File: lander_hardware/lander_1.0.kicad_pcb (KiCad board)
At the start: 2 copper layers, 76.2 x 63.5 mm, 45 parts, among them IC1 ATMEGA328-P, J1 Power Connector, J3 Pyro Channel, J4 Pyro Channel, J5 Pyro Channel, P1 Power Out, P2 ICSP, P3 XBEE Out, P4 Digital Supplement 1, P5 Digital Supplement 2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

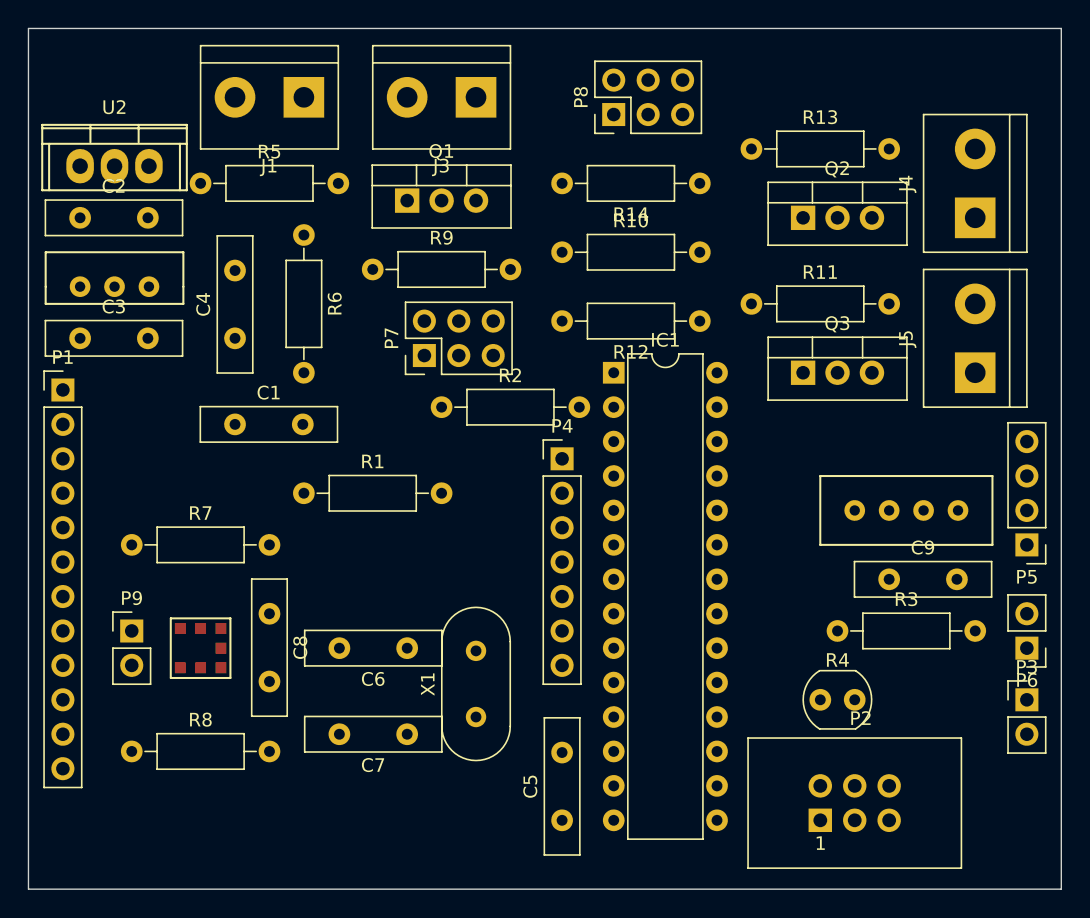
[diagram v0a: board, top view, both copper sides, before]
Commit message: Moved some decoupling caps closer
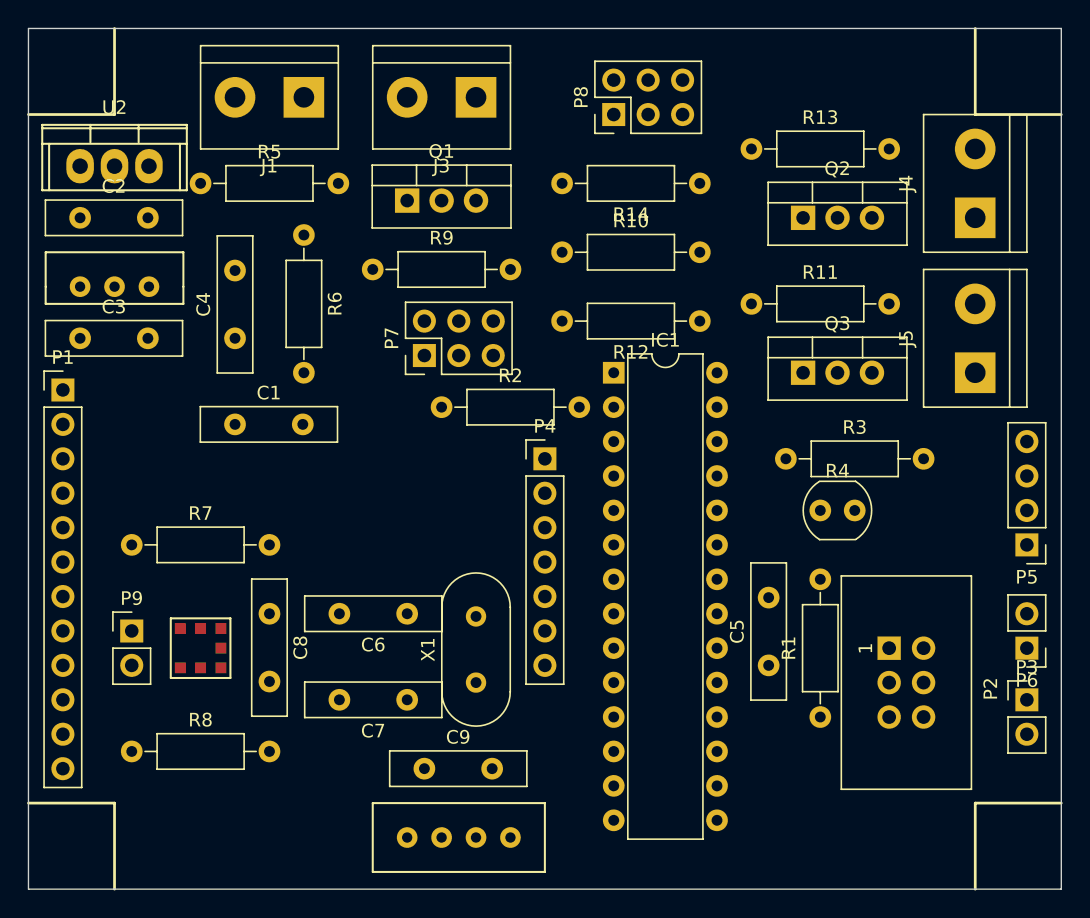
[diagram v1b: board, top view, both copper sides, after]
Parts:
- moved R1 41.5 mm to (196.8, 138.4), turned to 90 degrees
- moved U3 40.9 mm to (170.2, 147.3)
- moved C9 37.0 mm to (167.6, 142.2)
- moved C5 19.0 mm to (193.0, 134.6)
- moved R4 14.0 mm to (196.8, 123.2)
- moved P2 13.7 mm to (201.9, 133.3), turned to 270 degrees
- moved R3 13.3 mm to (194.3, 119.4)
- moved X1 2.54 mm to (171.4, 135.9)
- moved C6 2.54 mm to (166.4, 130.8)
- moved C7 2.54 mm to (166.4, 137.2)
- moved P4 1.27 mm to (176.5, 119.4)
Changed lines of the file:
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@@
     (links 117)
     (no_connects 117)
-    (area 137.912857 86.655 220.313811 152.125)
+    (area 136.912857 86.655 220.313811 152.125)
     (thickness 1.6)
-    (drawings 4)
+    (drawings 12)
     (tracks 0)
     (zones 0)
@@
   )
   (module Capacitors_THT:C_Disc_D10.0mm_W2.5mm_P5.00mm (layer F.Cu)
-    (at 177.8 146.05 90)
+    (at 193.04 134.62 90)
     (descr "C, Disc series, Radial, pin pitch=5.00mm, , diameter*width=10*2.5mm^2, Capacitor, http://cdn-reichelt.de/documents/datenblatt/B300/DS_KERKO_TC.pdf")
     (tags "C Disc series Radial pin pitch 5.00mm  diameter 10mm width 2.5mm Capacitor")
@@
   )
   (module Capacitors_THT:C_Disc_D10.0mm_W2.5mm_P5.00mm (layer F.Cu)
-    (at 166.37 133.35 180)
+    (at 166.37 130.81 180)
     (descr "C, Disc series, Radial, pin pitch=5.00mm, , diameter*width=10*2.5mm^2, Capacitor, http://cdn-reichelt.de/documents/datenblatt/B300/DS_KERKO_TC.pdf")
     (tags "C Disc series Radial pin pitch 5.00mm  diameter 10mm width 2.5mm Capacitor")
@@
   )
   (module Capacitors_THT:C_Disc_D10.0mm_W2.5mm_P5.00mm (layer F.Cu)
-    (at 166.37 139.7 180)
+    (at 166.37 137.16 180)
     (descr "C, Disc series, Radial, pin pitch=5.00mm, , diameter*width=10*2.5mm^2, Capacitor, http://cdn-reichelt.de/documents/datenblatt/B300/DS_KERKO_TC.pdf")
     (tags "C Disc series Radial pin pitch 5.00mm  diameter 10mm width 2.5mm Capacitor")
@@
   )
   (module Capacitors_THT:C_Disc_D10.0mm_W2.5mm_P5.00mm (layer F.Cu)
-    (at 201.93 128.27)
+    (at 167.64 142.24)
     (descr "C, Disc series, Radial, pin pitch=5.00mm, , diameter*width=10*2.5mm^2, Capacitor, http://cdn-reichelt.de/documents/datenblatt/B300/DS_KERKO_TC.pdf")
     (tags "C Disc series Radial pin pitch 5.00mm  diameter 10mm width 2.5mm Capacitor")
@@
   )
   (module Connectors:IDC_Header_Straight_6pins (layer F.Cu)
-    (at 196.85 146.05)
+    (at 201.93 133.35 270)
     (descr "6 pins through hole IDC header")
     (tags "IDC header socket VASCH AVR ISP")
-    (fp_text reference P2 (at 3 -7.5) (layer F.SilkS)
-      (effects (font (size 1 1) (thickness 0.15)))
-    )
-    (fp_text value ICSP (at 3 5) (layer F.Fab)
+    (fp_text reference P2 (at 3 -7.5 270) (layer F.SilkS)
+      (effects (font (size 1 1) (thickness 0.15)))
+    )
+    (fp_text value ICSP (at 3 5 270) (layer F.Fab)
       (effects (font (size 1 1) (thickness 0.15)))
     )
@@
     (fp_line (start 10.66 3.78) (end -5.58 3.78) (layer F.CrtYd) (width 0.05))
     (fp_line (start -5.58 3.78) (end -5.58 -6.32) (layer F.CrtYd) (width 0.05))
-    (fp_text user 1 (at 0.02 1.72) (layer F.SilkS)
+    (fp_text user 1 (at 0.02 1.72 270) (layer F.SilkS)
       (effects (font (size 1 1) (thickness 0.12)))
     )
@@
     (fp_line (start 10.41 3.53) (end -5.33 3.53) (layer F.SilkS) (width 0.12))
     (fp_line (start -5.33 3.53) (end -5.33 -6.07) (layer F.SilkS) (width 0.12))
-    (pad 1 thru_hole rect (at 0 0) (size 1.7272 1.7272) (drill 1.016) (layers *.Cu *.Mask)
+    (pad 1 thru_hole rect (at 0 0 270) (size 1.7272 1.7272) (drill 1.016) (layers *.Cu *.Mask)
       (net 14 "Net-(IC1-Pad18)"))
-    (pad 2 thru_hole oval (at 0 -2.54) (size 1.7272 1.7272) (drill 1.016) (layers *.Cu *.Mask)
+    (pad 2 thru_hole oval (at 0 -2.54 270) (size 1.7272 1.7272) (drill 1.016) (layers *.Cu *.Mask)
       (net 4 +5V))
-    (pad 3 thru_hole oval (at 2.54 0) (size 1.7272 1.7272) (drill 1.016) (layers *.Cu *.Mask)
+    (pad 3 thru_hole oval (at 2.54 0 270) (size 1.7272 1.7272) (drill 1.016) (layers *.Cu *.Mask)
       (net 16 "Net-(IC1-Pad19)"))
-    (pad 4 thru_hole oval (at 2.54 -2.54) (size 1.7272 1.7272) (drill 1.016) (layers *.Cu *.Mask)
+    (pad 4 thru_hole oval (at 2.54 -2.54 270) (size 1.7272 1.7272) (drill 1.016) (layers *.Cu *.Mask)
       (net 12 "Net-(IC1-Pad17)"))
-    (pad 5 thru_hole oval (at 5.08 0) (size 1.7272 1.7272) (drill 1.016) (layers *.Cu *.Mask)
+    (pad 5 thru_hole oval (at 5.08 0 270) (size 1.7272 1.7272) (drill 1.016) (layers *.Cu *.Mask)
       (net 7 "Net-(IC1-Pad1)"))
-    (pad 6 thru_hole oval (at 5.08 -2.54) (size 1.7272 1.7272) (drill 1.016) (layers *.Cu *.Mask)
+    (pad 6 thru_hole oval (at 5.08 -2.54 270) (size 1.7272 1.7272) (drill 1.016) (layers *.Cu *.Mask)
       (net 2 GND))
   )
@@
   )
   (module Pin_Headers:Pin_Header_Straight_1x07_Pitch2.54mm (layer F.Cu)
-    (at 177.8 119.38)
+    (at 176.53 119.38)
     (descr "Through hole straight pin header, 1x07, 2.54mm pitch, single row")
     (tags "Through hole pin header THT 1x07 2.54mm single row")
@@
   )
   (module Resistors_THT:R_Axial_DIN0207_L6.3mm_D2.5mm_P10.16mm_Horizontal (layer F.Cu)
-    (at 158.75 121.92)
+    (at 196.85 138.43 90)
     (descr "Resistor, Axial_DIN0207 series, Axial, Horizontal, pin pitch=10.16mm, 0.25W = 1/4W, length*diameter=6.3*2.5mm^2, http://cdn-reichelt.de/documents/datenblatt/B400/1_4W%23YAG.pdf")
     (tags "Resistor Axial_DIN0207 series Axial Horizontal pin pitch 10.16mm 0.25W = 1/4W length 6.3mm diameter 2.5mm")
-    (fp_text reference R1 (at 5.08 -2.31) (layer F.SilkS)
-      (effects (font (size 1 1) (thickness 0.15)))
-    )
-    (fp_text value 10K (at 5.08 2.31) (layer F.Fab)
+    (fp_text reference R1 (at 5.08 -2.31 90) (layer F.SilkS)
+      (effects (font (size 1 1) (thickness 0.15)))
+    )
+    (fp_text value 10K (at 5.08 2.31 90) (layer F.Fab)
       (effects (font (size 1 1) (thickness 0.15)))
     )
@@
     (fp_line (start 11.25 1.6) (end 11.25 -1.6) (layer F.CrtYd) (width 0.05))
     (fp_line (start 11.25 -1.6) (end -1.05 -1.6) (layer F.CrtYd) (width 0.05))
-    (pad 1 thru_hole circle (at 0 0) (size 1.6 1.6) (drill 0.8) (layers *.Cu *.Mask)
+    (pad 1 thru_hole circle (at 0 0 90) (size 1.6 1.6) (drill 0.8) (layers *.Cu *.Mask)
       (net 4 +5V))
-    (pad 2 thru_hole oval (at 10.16 0) (size 1.6 1.6) (drill 0.8) (layers *.Cu *.Mask)
+    (pad 2 thru_hole oval (at 10.16 0 90) (size 1.6 1.6) (drill 0.8) (layers *.Cu *.Mask)
       (net 18 "Net-(IC1-Pad21)"))
     (model Resistors_THT.3dshapes/R_Axial_DIN0207_L6.3mm_D2.5mm_P10.16mm_Horizontal.wrl
@@
   )
   (module Resistors_THT:R_Axial_DIN0207_L6.3mm_D2.5mm_P10.16mm_Horizontal (layer F.Cu)
-    (at 198.12 132.08)
+    (at 194.31 119.38)
     (descr "Resistor, Axial_DIN0207 series, Axial, Horizontal, pin pitch=10.16mm, 0.25W = 1/4W, length*diameter=6.3*2.5mm^2, http://cdn-reichelt.de/documents/datenblatt/B400/1_4W%23YAG.pdf")
     (tags "Resistor Axial_DIN0207 series Axial Horizontal pin pitch 10.16mm 0.25W = 1/4W length 6.3mm diameter 2.5mm")
@@
   )
   (module Opto-Devices:Resistor_LDR_4.9x4.2_RM2.54 (layer F.Cu)
-    (at 196.85 137.16)
+    (at 196.85 123.19)
     (descr "Resistor, LDR 4.9x4.2mm")
     (tags "Resistor LDR4.9x4.2")
@@
   )
   (module footprints:dht11 (layer F.Cu)
-    (at 203.2 123.19)
+    (at 170.18 147.32)
     (fp_text reference U3 (at 0 2.54) (layer F.SilkS) hide
       (effects (font (size 1 1) (thickness 0.15)))
@@
   )
   (module Crystals:Crystal_HC49-U_Vertical (layer F.Cu)
-    (at 171.45 138.43 90)
+    (at 171.45 135.89 90)
     (descr "Crystal THT HC-49/U http://5hertz.com/pdfs/04404_D.pdf")
     (tags "THT crystalHC-49/U")
@@
       (net 40 "Net-(U4-Pad7)"))
   )
+  (gr_line (start 144.78 144.78) (end 138.43 144.78) (angle 90) (layer F.SilkS) (width 0.2))
+  (gr_line (start 144.78 151.13) (end 144.78 144.78) (angle 90) (layer F.SilkS) (width 0.2))
+  (gr_line (start 208.28 144.78) (end 214.63 144.78) (angle 90) (layer F.SilkS) (width 0.2))
+  (gr_line (start 208.28 151.13) (end 208.28 144.78) (angle 90) (layer F.SilkS) (width 0.2))
+  (gr_line (start 208.28 93.98) (end 208.28 87.63) (angle 90) (layer F.SilkS) (width 0.2))
+  (gr_line (start 214.63 93.98) (end 208.28 93.98) (angle 90) (layer F.SilkS) (width 0.2))
+  (gr_line (start 144.78 93.98) (end 144.78 87.63) (angle 90) (layer F.SilkS) (width 0.2))
+  (gr_line (start 138.43 93.98) (end 144.78 93.98) (angle 90) (layer F.SilkS) (width 0.2))
   (gr_line (start 138.43 151.13) (end 138.43 87.63) (angle 90) (layer Edge.Cuts) (width 0.1))
   (gr_line (start 214.63 151.13) (end 138.43 151.13) (angle 90) (layer Edge.Cuts) (width 0.1))

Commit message: Updated constraints
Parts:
- moved R9 1.27 mm to (162.6, 105.4)
- moved P8 1.27 mm to (181.6, 95.2)
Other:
- net class 6V Power added: clearance 0.2, trace_width 0.8, via_dia 0.6, via_drill 0.4
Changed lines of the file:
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@@
     (links 117)
     (no_connects 117)
-    (area 136.912857 86.655 220.313811 152.125)
+    (area 136.912857 86.655 220.313811 151.230001)
     (thickness 1.6)
     (drawings 12)
@@
     (add_net +3V3)
     (add_net +5V)
-    (add_net +6V)
     (add_net "/Altimeter I2C/SCL")
     (add_net "/Altimeter I2C/SDA")
@@
     (add_net "Net-(U4-Pad7)")
   )
+  (net_class "6V Power" ""
+    (clearance 0.2)
+    (trace_width 0.8)
+    (via_dia 0.6)
+    (via_drill 0.4)
+    (uvia_dia 0.3)
+    (uvia_drill 0.1)
+    (add_net +6V)
+  )
   (module Capacitors_THT:C_Disc_D10.0mm_W2.5mm_P5.00mm (layer F.Cu)
     (at 153.67 116.84)
@@
     (descr "28-lead dip package, row spacing 7.62 mm (300 mils)")
     (tags "DIL DIP PDIP 2.54mm 7.62mm 300mil")
-    (fp_text reference IC1 (at 3.81 -2.39) (layer F.SilkS)
+    (fp_text reference IC1 (at 3.81 1.27) (layer F.SilkS)
       (effects (font (size 1 1) (thickness 0.15)))
     )
@@
   )
   (module Pin_Headers:Pin_Header_Straight_2x03_Pitch2.54mm (layer F.Cu)
-    (at 181.61 93.98 90)
+    (at 181.61 95.25 90)
     (descr "Through hole straight pin header, 2x03, 2.54mm pitch, double rows")
     (tags "Through hole pin header THT 2x03 2.54mm double row")
@@
   )
   (module Resistors_THT:R_Axial_DIN0207_L6.3mm_D2.5mm_P10.16mm_Horizontal (layer F.Cu)
-    (at 163.83 105.41)
+    (at 162.56 105.41)
     (descr "Resistor, Axial_DIN0207 series, Axial, Horizontal, pin pitch=10.16mm, 0.25W = 1/4W, length*diameter=6.3*2.5mm^2, http://cdn-reichelt.de/documents/datenblatt/B400/1_4W%23YAG.pdf")
     (tags "Resistor Axial_DIN0207 series Axial Horizontal pin pitch 10.16mm 0.25W = 1/4W length 6.3mm diameter 2.5mm")
@@
     (descr "Resistor, Axial_DIN0207 series, Axial, Horizontal, pin pitch=10.16mm, 0.25W = 1/4W, length*diameter=6.3*2.5mm^2, http://cdn-reichelt.de/documents/datenblatt/B400/1_4W%23YAG.pdf")
     (tags "Resistor Axial_DIN0207 series Axial Horizontal pin pitch 10.16mm 0.25W = 1/4W length 6.3mm diameter 2.5mm")
-    (fp_text reference R10 (at 5.08 -2.31) (layer F.SilkS)
+    (fp_text reference R10 (at 5.08 0) (layer F.SilkS)
       (effects (font (size 1 1) (thickness 0.15)))
     )
@@
     (descr "Resistor, Axial_DIN0207 series, Axial, Horizontal, pin pitch=10.16mm, 0.25W = 1/4W, length*diameter=6.3*2.5mm^2, http://cdn-reichelt.de/documents/datenblatt/B400/1_4W%23YAG.pdf")
     (tags "Resistor Axial_DIN0207 series Axial Horizontal pin pitch 10.16mm 0.25W = 1/4W length 6.3mm diameter 2.5mm")
-    (fp_text reference R12 (at 5.08 -2.31 180) (layer F.SilkS)
+    (fp_text reference R12 (at 5.08 0 180) (layer F.SilkS)
       (effects (font (size 1 1) (thickness 0.15)))
     )
@@
     (descr "Resistor, Axial_DIN0207 series, Axial, Horizontal, pin pitch=10.16mm, 0.25W = 1/4W, length*diameter=6.3*2.5mm^2, http://cdn-reichelt.de/documents/datenblatt/B400/1_4W%23YAG.pdf")
     (tags "Resistor Axial_DIN0207 series Axial Horizontal pin pitch 10.16mm 0.25W = 1/4W length 6.3mm diameter 2.5mm")
-    (fp_text reference R14 (at 5.08 -2.31 180) (layer F.SilkS)
-      (effects (font (size 1 1) (thickness 0.15)))
-    )
+    (fp_text reference R14 (at 5.08 0 180) (layer F.SilkS)
+      (effects (font (size 1 1) (thickness 0.15)))
+    )

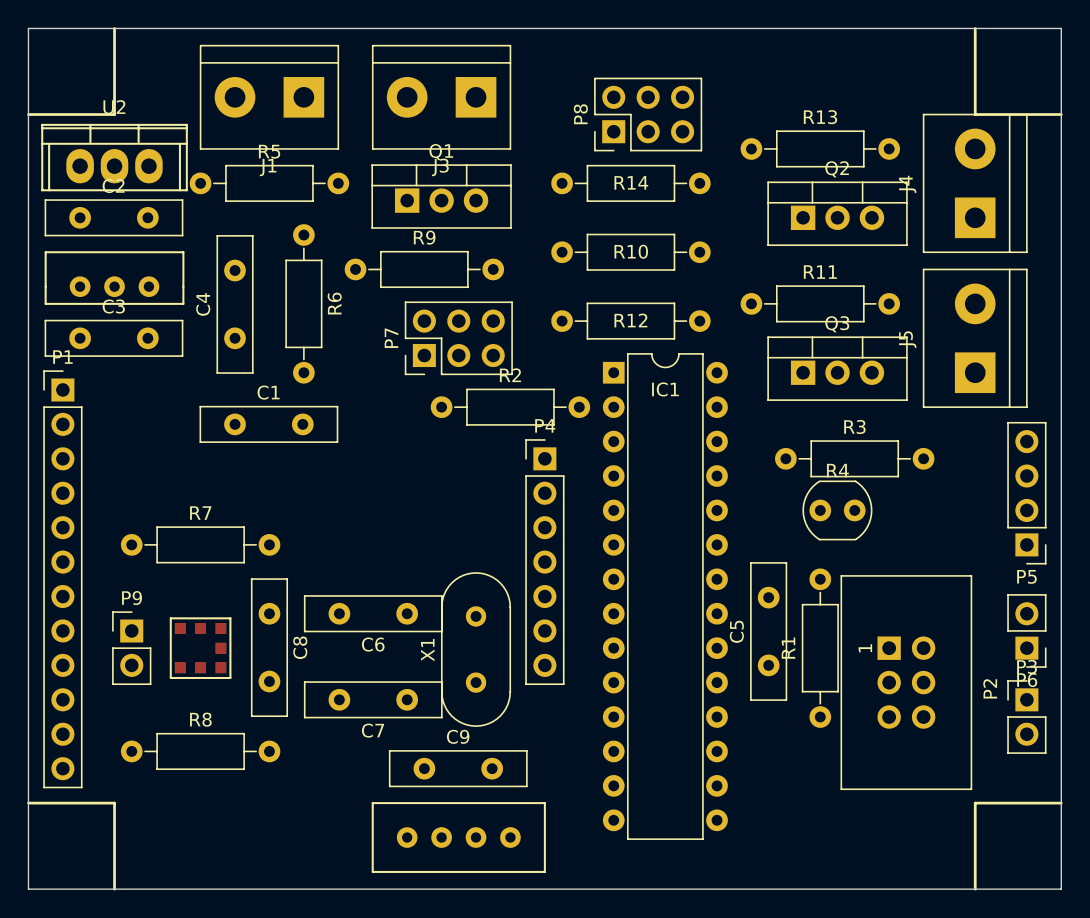
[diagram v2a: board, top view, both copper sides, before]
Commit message: Track width, via size, screws
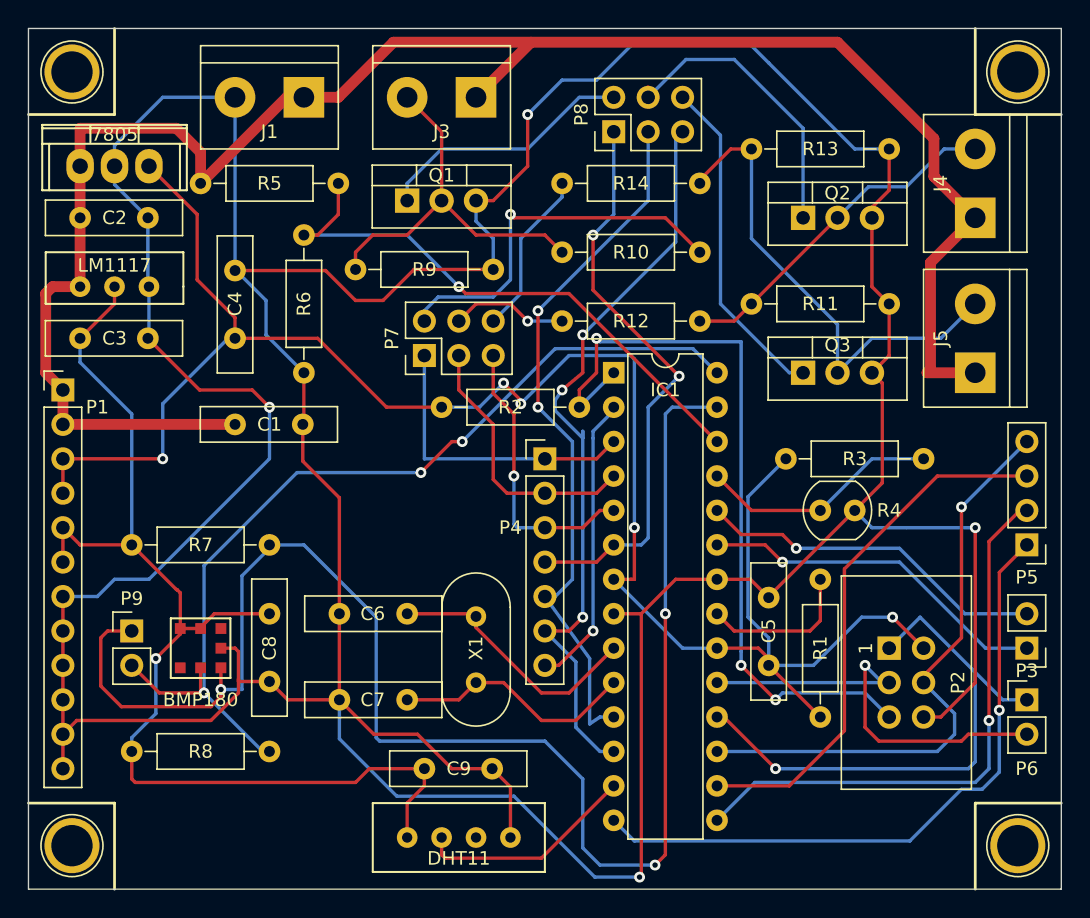
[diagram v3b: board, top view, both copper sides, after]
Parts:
- added REF**: 1pin, Connectors:1pin, F.Cu at (141.6, 90.8)
- added REF**: 1pin, Connectors:1pin, F.Cu at (211.4, 90.8)
- added REF**: 1pin, Connectors:1pin, F.Cu at (141.6, 147.9)
- added REF**: 1pin, Connectors:1pin, F.Cu at (211.4, 147.9)
- Q1, Q2, Q3: value Q_NPN_CBE -> Q_NPN_BCE
- renumbered U2 to 7805, U4 to BMP180, U3 to DHT11, U1 to LM1117
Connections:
- Q1 pad 1: Net-(J3-Pad2) -> Net-(P8-Pad2)
- Q1 pad 2: Net-(P8-Pad2) -> Net-(J3-Pad2)
- Q2 pad 1: Net-(J4-Pad2) -> Net-(P8-Pad4)
- Q2 pad 2: Net-(P8-Pad4) -> Net-(J4-Pad2)
- Q3 pad 1: Net-(J5-Pad2) -> Net-(P8-Pad6)
- Q3 pad 2: Net-(P8-Pad6) -> Net-(J5-Pad2)
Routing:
- net GND: track 0.00 -> 359.6 mm, vias 0 -> 4
- net +6V: track 0.00 -> 139.9 mm
- net +5V: track 0.00 -> 139.7 mm, vias 0 -> 5
- net /Altimeter I2C/SDA: track 0.00 -> 115.1 mm, vias 0 -> 3
- net +3V3: track 0.00 -> 84.9 mm, vias 0 -> 1
- net /Altimeter I2C/SCL: track 0.00 -> 69.4 mm, vias 0 -> 3
- net Net-(IC1-Pad1): track 0.00 -> 56.8 mm, vias 0 -> 3
- net /Pyro Channels/Pyro3: track 0.00 -> 56.4 mm, vias 0 -> 3
- net /Pyro Channels/Pyro2: track 0.00 -> 52.4 mm, vias 0 -> 2
- net Net-(IC1-Pad14): track 0.00 -> 48.8 mm, vias 0 -> 1
- net Net-(IC1-Pad17): track 0.00 -> 43.7 mm, vias 0 -> 1
- net /Pyro Channels/Pyro1: track 0.00 -> 42.5 mm, vias 0 -> 2
- net Net-(IC1-Pad26): track 0.00 -> 42.2 mm, vias 0 -> 1
- net Net-(IC1-Pad15): track 0.00 -> 42.1 mm, vias 0 -> 1
- net Net-(IC1-Pad18): track 0.00 -> 41.8 mm, vias 0 -> 1
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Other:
- net class 6V Power: via_dia 0.6 -> 0.8
- net class Default: via_dia 0.6 -> 0.8
